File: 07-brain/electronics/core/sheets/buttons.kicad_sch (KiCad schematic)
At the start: 0 parts

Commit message: Brain schematics WIP
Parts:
- added R16, R17: 470, Resistor_SMD:R_0603_1608Metric, symbol Device:R
- added U10, U2: SW_SPST_Push_LED, Shmoergh_Custom_Footprints:SPST_Circular_Pushbutton_LED, symbol Shmoergh-Custom-Components:SW_SPST_Push_LED
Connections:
- new net: R17.2, U10.L1
- new net: R16.2, U2.L1
- new net BTN1: U2.2
- new net BTN1_LED: R16.1
- new net BTN2: U10.2
- new net BTN2_LED: R17.1
- new net GND: U10.4, U10.L2, U2.4, U2.L2
- no-connect marks 0 -> 4

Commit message: Updated Brain schematics
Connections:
- net BTN1 renamed BTN_1
- net BTN1_LED renamed BTN_1_LED
- net BTN2 renamed BTN_2
- net BTN2_LED renamed BTN_2_LED
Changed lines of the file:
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@@
 		)
 	)
-	(hierarchical_label "BTN2_LED"
+	(hierarchical_label "BTN_2_LED"
 		(shape input)
 		(at 161.29 87.63 180)
@@
 		)
 	)
-	(hierarchical_label "BTN2"
+	(hierarchical_label "BTN_2"
 		(shape output)
 		(at 199.39 78.74 0)
@@
 		)
 	)
-	(hierarchical_label "BTN1_LED"
+	(hierarchical_label "BTN_1_LED"
 		(shape input)
 		(at 95.25 87.63 180)
@@
 		)
 	)
-	(hierarchical_label "BTN1"
+	(hierarchical_label "BTN_1"
 		(shape output)
 		(at 133.35 78.74 0)

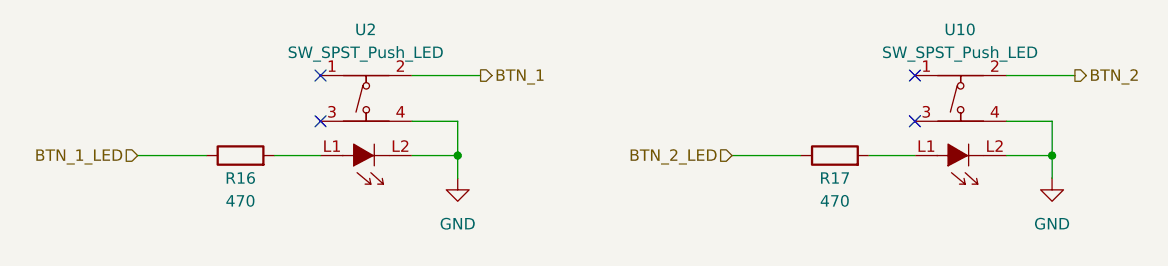
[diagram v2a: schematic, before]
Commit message: Audio/CV out BrainSDK tested/working
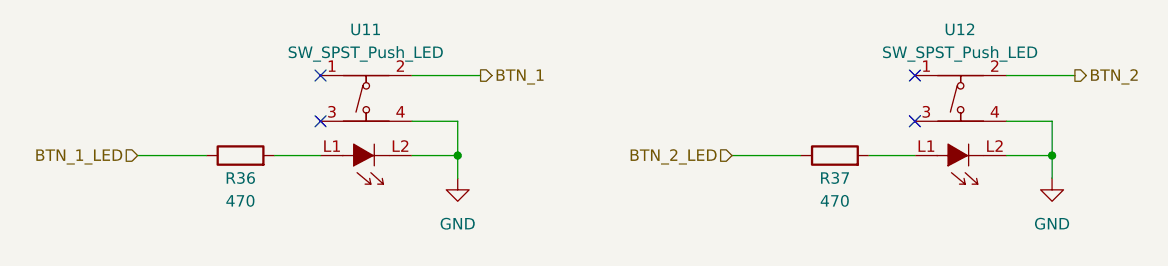
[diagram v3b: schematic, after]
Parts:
- renumbered R16 to R36, R17 to R37, U2 to U11, U10 to U12
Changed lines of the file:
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@@
 		(dnp no)
 		(fields_autoplaced yes)
-		(property "Reference" "U10"
+		(property "Reference" "U12"
 			(at 186.6265 73.66 0)
 			(effects
@@
 			(project "brain-core"
 				(path "/8e2e31f3-eed5-4de1-966c-f4162758c735/a97d408f-9e6e-4f2a-a0b2-91646f8dc854"
-					(reference "U10")
+					(reference "U12")
 					(unit 1)
 				)
@@
 		(dnp no)
 		(fields_autoplaced yes)
-		(property "Reference" "U2"
+		(property "Reference" "U11"
 			(at 120.5865 73.66 0)
 			(effects
@@
 			(project "brain-core"
 				(path "/8e2e31f3-eed5-4de1-966c-f4162758c735/a97d408f-9e6e-4f2a-a0b2-91646f8dc854"
-					(reference "U2")
+					(reference "U11")
 					(unit 1)
 				)
@@
 		(dnp no)
 		(fields_autoplaced yes)
-		(property "Reference" "#PWR068"
+		(property "Reference" "#PWR071"
 			(at 196.85 96.52 0)
 			(effects
@@
 			(project "brain-core"
 				(path "/8e2e31f3-eed5-4de1-966c-f4162758c735/a97d408f-9e6e-4f2a-a0b2-91646f8dc854"
-					(reference "#PWR068")
+					(reference "#PWR071")
 					(unit 1)
 				)
@@
 		(dnp no)
 		(fields_autoplaced yes)
-		(property "Reference" "#PWR067"
+		(property "Reference" "#PWR070"
 			(at 130.81 96.52 0)
 			(effects
@@
 			(project ""
 				(path "/8e2e31f3-eed5-4de1-966c-f4162758c735/a97d408f-9e6e-4f2a-a0b2-91646f8dc854"
-					(reference "#PWR067")
+					(reference "#PWR070")
 					(unit 1)
 				)
@@
 		(on_board yes)
 		(dnp no)
-		(property "Reference" "R17"
+		(property "Reference" "R37"
 			(at 172.72 90.17 90)
 			(effects
@@
 			(project "brain-core"
 				(path "/8e2e31f3-eed5-4de1-966c-f4162758c735/a97d408f-9e6e-4f2a-a0b2-91646f8dc854"
-					(reference "R17")
+					(reference "R37")
 					(unit 1)
 				)
@@
 		(on_board yes)
 		(dnp no)
-		(property "Reference" "R16"
+		(property "Reference" "R36"
 			(at 106.68 90.17 90)
 			(effects
@@
 			(project "brain-core"
 				(path "/8e2e31f3-eed5-4de1-966c-f4162758c735/a97d408f-9e6e-4f2a-a0b2-91646f8dc854"
-					(reference "R16")
+					(reference "R36")
 					(unit 1)
 				)

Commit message: Design Brain/Core PCB
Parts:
- removed R37: 470, Resistor_SMD:R_0603_1608Metric, symbol Device:R
- removed U12: SW_SPST_Push_LED, Shmoergh_Custom_Footprints:SPST_Circular_Pushbutton_LED, symbol Shmoergh-Custom-Components:SW_SPST_Push_LED
- added #R1: 470, Resistor_SMD:R_0603_1608Metric, symbol Device:R
- added #U1: SW_SPST_Push_LED, Shmoergh_Custom_Footprints:SPST_Circular_Pushbutton_LED, symbol Shmoergh-Custom-Components:SW_SPST_Push_LED
- renumbered R36 to #R36, U11 to #U11
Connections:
- net GND: now also #U1.4, #U1.L2
- net BTN_1: no longer names the net of #U11.2
- net BTN_1_LED: no longer names the net of #R36.1
- new net: #R1.2, #U1.L1
- no-connect marks 4 -> 8
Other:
- note added: "BTN_1"
- note added: "BTN_2"
- note added: "BTN_LED_1"
- note added: "BTN_LED_2"
